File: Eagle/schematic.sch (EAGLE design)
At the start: 4 parts, among them IC1 ATMEGA328-20P

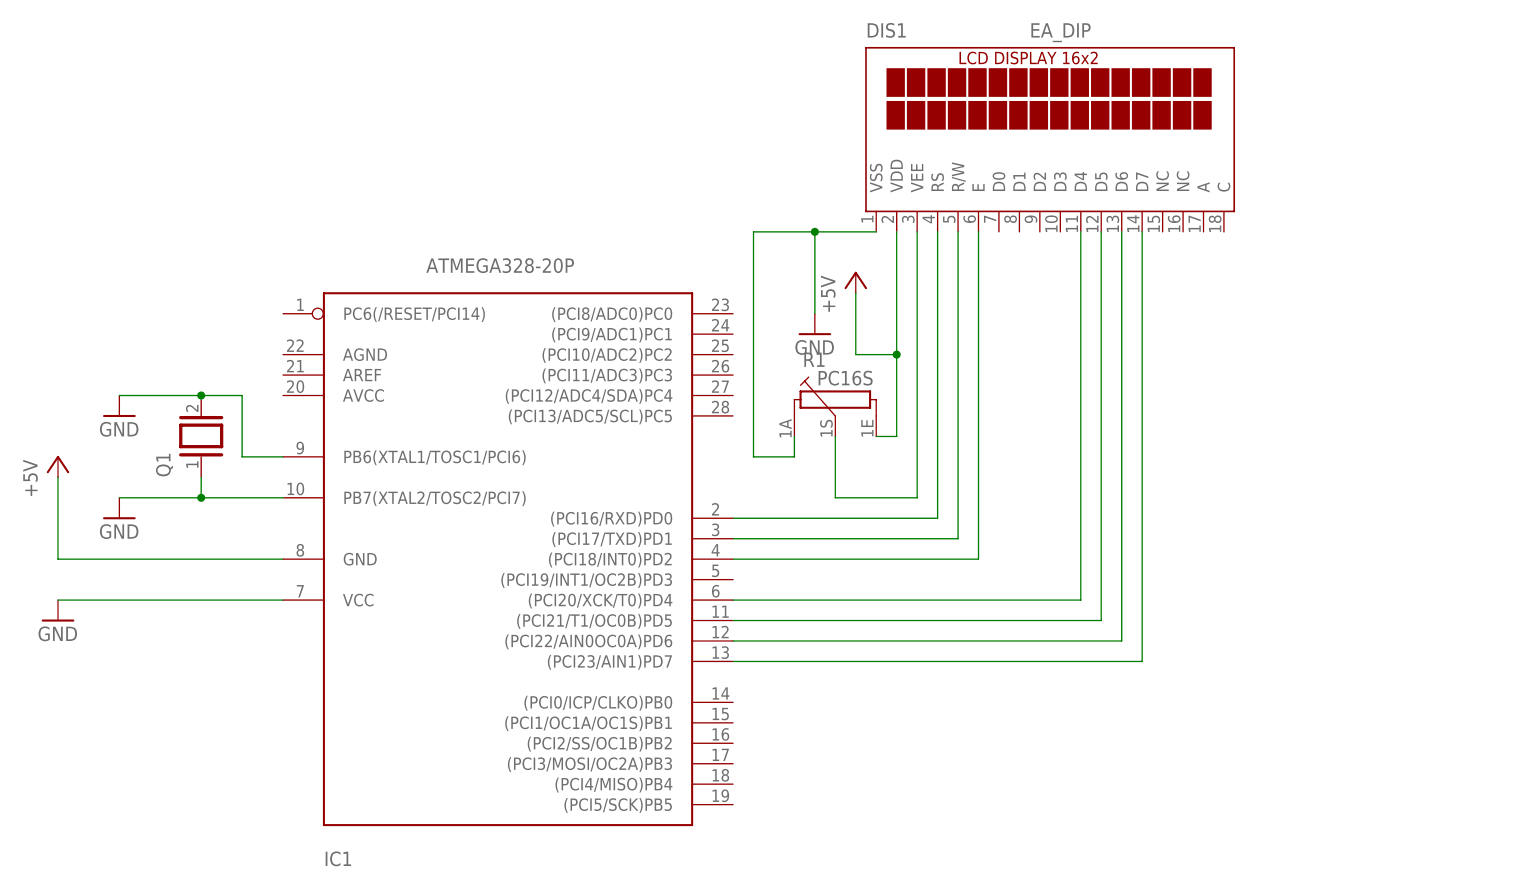
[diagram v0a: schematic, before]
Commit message: Add schematic file to the project
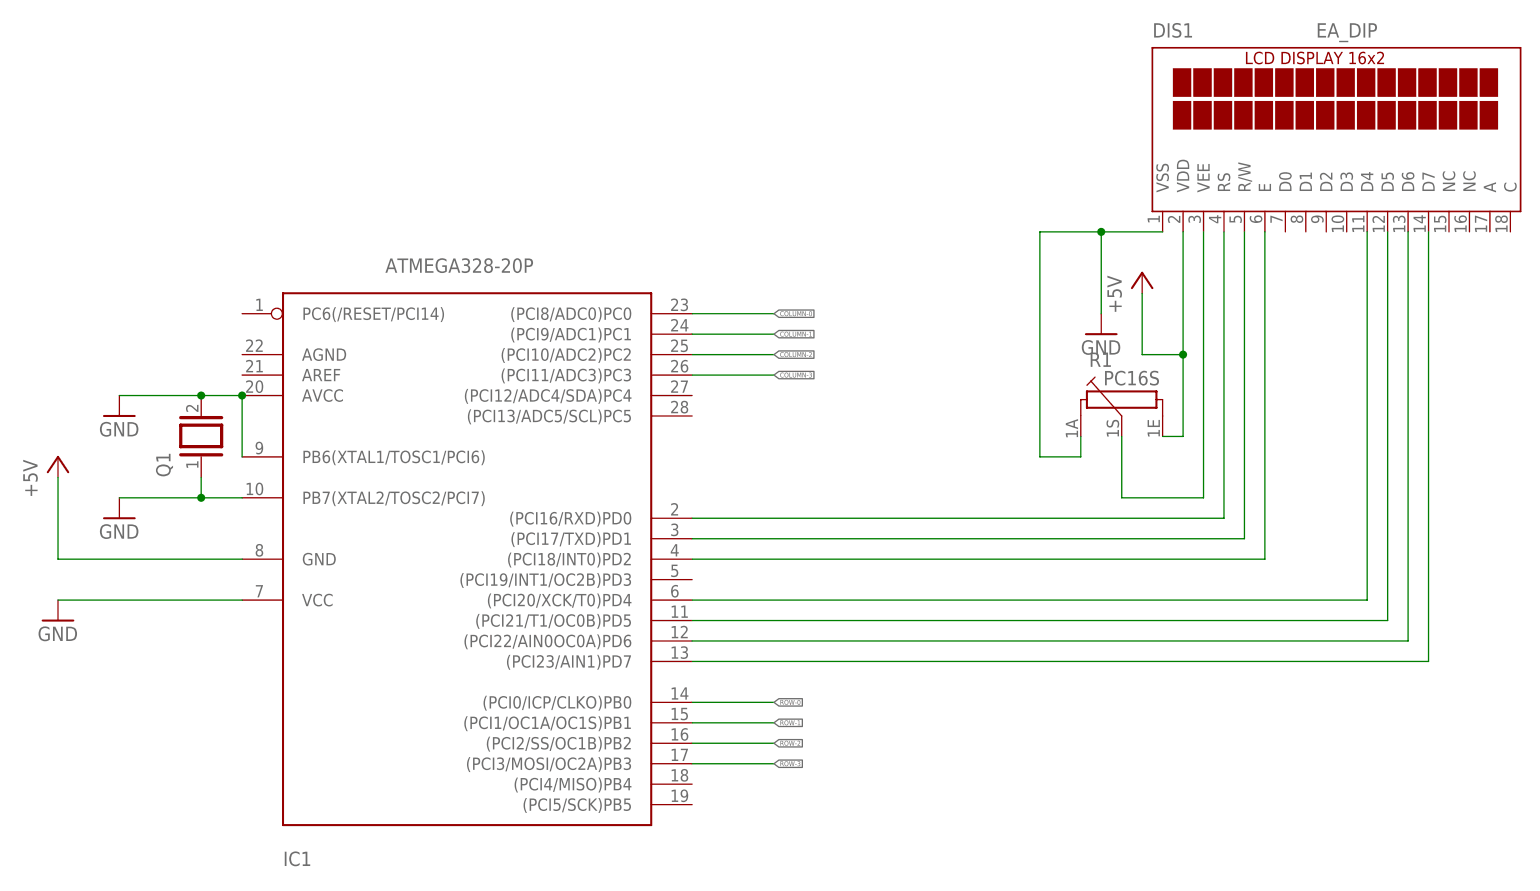
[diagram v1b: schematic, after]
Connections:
- net GND: now also IC1.AVCC
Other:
- moved on the sheet: DIS1, IC1, R1
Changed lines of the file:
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@@
 </plain>
 <instances>
-<instance part="IC1" gate="G$1" x="63.5" y="55.88"/>
-<instance part="DIS1" gate="G$1" x="134.62" y="104.14"/>
+<instance part="IC1" gate="G$1" x="58.42" y="55.88"/>
+<instance part="DIS1" gate="G$1" x="170.18" y="104.14"/>
 <instance part="GND1" gate="1" x="12.7" y="45.72"/>
 <instance part="P+1" gate="1" x="12.7" y="66.04"/>
-<instance part="P+2" gate="1" x="111.76" y="88.9"/>
-<instance part="GND2" gate="1" x="106.68" y="81.28"/>
-<instance part="R1" gate="G$1" x="109.22" y="73.66"/>
+<instance part="P+2" gate="1" x="147.32" y="88.9"/>
+<instance part="GND2" gate="1" x="142.24" y="81.28"/>
+<instance part="R1" gate="G$1" x="144.78" y="73.66"/>
 <instance part="Q1" gate="G$1" x="30.48" y="68.58" rot="R90"/>
 <instance part="GND3" gate="1" x="20.32" y="58.42"/>
@@
 <segment>
 <pinref part="IC1" gate="G$1" pin="VCC"/>
-<wire x1="40.64" y1="48.26" x2="12.7" y2="48.26" width="0.1524" layer="91"/>
+<wire x1="35.56" y1="48.26" x2="12.7" y2="48.26" width="0.1524" layer="91"/>
 <pinref part="GND1" gate="1" pin="GND"/>
 </segment>
@@
 <pinref part="DIS1" gate="G$1" pin="VSS"/>
 <pinref part="GND2" gate="1" pin="GND"/>
-<wire x1="114.3" y1="93.98" x2="106.68" y2="93.98" width="0.1524" layer="91"/>
-<wire x1="106.68" y1="93.98" x2="106.68" y2="83.82" width="0.1524" layer="91"/>
-<wire x1="106.68" y1="93.98" x2="99.06" y2="93.98" width="0.1524" layer="91"/>
-<junction x="106.68" y="93.98"/>
-<wire x1="99.06" y1="93.98" x2="99.06" y2="66.04" width="0.1524" layer="91"/>
-<wire x1="99.06" y1="66.04" x2="104.14" y2="66.04" width="0.1524" layer="91"/>
+<wire x1="149.86" y1="93.98" x2="142.24" y2="93.98" width="0.1524" layer="91"/>
+<wire x1="142.24" y1="93.98" x2="142.24" y2="83.82" width="0.1524" layer="91"/>
+<wire x1="142.24" y1="93.98" x2="134.62" y2="93.98" width="0.1524" layer="91"/>
+<junction x="142.24" y="93.98"/>
+<wire x1="134.62" y1="93.98" x2="134.62" y2="66.04" width="0.1524" layer="91"/>
+<wire x1="134.62" y1="66.04" x2="139.7" y2="66.04" width="0.1524" layer="91"/>
 <pinref part="R1" gate="G$1" pin="1A"/>
-<wire x1="104.14" y1="66.04" x2="104.14" y2="68.58" width="0.1524" layer="91"/>
+<wire x1="139.7" y1="66.04" x2="139.7" y2="68.58" width="0.1524" layer="91"/>
 </segment>
 <segment>
 <pinref part="IC1" gate="G$1" pin="PB6(XTAL1/TOSC1/PCI6)"/>
-<wire x1="40.64" y1="66.04" x2="35.56" y2="66.04" width="0.1524" layer="91"/>
 <wire x1="35.56" y1="66.04" x2="35.56" y2="73.66" width="0.1524" layer="91"/>
 <pinref part="Q1" gate="G$1" pin="2"/>
@@
 <pinref part="GND4" gate="1" pin="GND"/>
 <wire x1="30.48" y1="73.66" x2="20.32" y2="73.66" width="0.1524" layer="91"/>
+<pinref part="IC1" gate="G$1" pin="AVCC"/>
+<junction x="35.56" y="73.66"/>
 </segment>
 <segment>
 <pinref part="IC1" gate="G$1" pin="PB7(XTAL2/TOSC2/PCI7)"/>
 <pinref part="Q1" gate="G$1" pin="1"/>
-<wire x1="40.64" y1="60.96" x2="30.48" y2="60.96" width="0.1524" layer="91"/>
+<wire x1="35.56" y1="60.96" x2="30.48" y2="60.96" width="0.1524" layer="91"/>
 <wire x1="30.48" y1="60.96" x2="30.48" y2="63.5" width="0.1524" layer="91"/>
 <pinref part="GND3" gate="1" pin="GND"/>
@@
 <segment>
 <pinref part="IC1" gate="G$1" pin="GND"/>
-<wire x1="40.64" y1="53.34" x2="12.7" y2="53.34" width="0.1524" layer="91"/>
+<wire x1="35.56" y1="53.34" x2="12.7" y2="53.34" width="0.1524" layer="91"/>
 <wire x1="12.7" y1="53.34" x2="12.7" y2="63.5" width="0.1524" layer="91"/>
 <pinref part="P+1" gate="1" pin="+5V"/>
@@
 <segment>
 <pinref part="DIS1" gate="G$1" pin="VDD"/>
-<wire x1="116.84" y1="93.98" x2="116.84" y2="78.74" width="0.1524" layer="91"/>
-<wire x1="116.84" y1="78.74" x2="111.76" y2="78.74" width="0.1524" layer="91"/>
+<wire x1="152.4" y1="93.98" x2="152.4" y2="78.74" width="0.1524" layer="91"/>
+<wire x1="152.4" y1="78.74" x2="147.32" y2="78.74" width="0.1524" layer="91"/>
 <pinref part="P+2" gate="1" pin="+5V"/>
-<wire x1="111.76" y1="78.74" x2="111.76" y2="86.36" width="0.1524" layer="91"/>
+<wire x1="147.32" y1="78.74" x2="147.32" y2="86.36" width="0.1524" layer="91"/>
 <pinref part="R1" gate="G$1" pin="1E"/>
-<wire x1="114.3" y1="68.58" x2="116.84" y2="68.58" width="0.1524" layer="91"/>
-<wire x1="116.84" y1="68.58" x2="116.84" y2="78.74" width="0.1524" layer="91"/>
-<junction x="116.84" y="78.74"/>
+<wire x1="149.86" y1="68.58" x2="152.4" y2="68.58" width="0.1524" layer="91"/>
+<wire x1="152.4" y1="68.58" x2="152.4" y2="78.74" width="0.1524" layer="91"/>
+<junction x="152.4" y="78.74"/>
 </segment>
 </net>
@@
 <pinref part="IC1" gate="G$1" pin="(PCI16/RXD)PD0"/>
 <pinref part="DIS1" gate="G$1" pin="RS"/>
-<wire x1="96.52" y1="58.42" x2="121.92" y2="58.42" width="0.1524" layer="91"/>
-<wire x1="121.92" y1="58.42" x2="121.92" y2="93.98" width="0.1524" layer="91"/>
+<wire x1="91.44" y1="58.42" x2="157.48" y2="58.42" width="0.1524" layer="91"/>
+<wire x1="157.48" y1="58.42" x2="157.48" y2="93.98" width="0.1524" layer="91"/>
 </segment>
 </net>
@@
 <pinref part="IC1" gate="G$1" pin="(PCI17/TXD)PD1"/>
 <pinref part="DIS1" gate="G$1" pin="R/W"/>
-<wire x1="96.52" y1="55.88" x2="124.46" y2="55.88" width="0.1524" layer="91"/>
-<wire x1="124.46" y1="55.88" x2="124.46" y2="93.98" width="0.1524" layer="91"/>
+<wire x1="91.44" y1="55.88" x2="160.02" y2="55.88" width="0.1524" layer="91"/>
+<wire x1="160.02" y1="55.88" x2="160.02" y2="93.98" width="0.1524" layer="91"/>
 </segment>
 </net>
@@
 <pinref part="IC1" gate="G$1" pin="(PCI18/INT0)PD2"/>
 <pinref part="DIS1" gate="G$1" pin="E"/>
-<wire x1="96.52" y1="53.34" x2="127" y2="53.34" width="0.1524" layer="91"/>
-<wire x1="127" y1="53.34" x2="127" y2="93.98" width="0.1524" layer="91"/>
+<wire x1="91.44" y1="53.34" x2="162.56" y2="53.34" width="0.1524" layer="91"/>
+<wire x1="162.56" y1="53.34" x2="162.56" y2="93.98" width="0.1524" layer="91"/>
 </segment>
 </net>
@@
 <pinref part="IC1" gate="G$1" pin="(PCI23/AIN1)PD7"/>
 <pinref part="DIS1" gate="G$1" pin="D7"/>
-<wire x1="96.52" y1="40.64" x2="147.32" y2="40.64" width="0.1524" layer="91"/>
-<wire x1="147.32" y1="40.64" x2="147.32" y2="93.98" width="0.1524" layer="91"/>
+<wire x1="91.44" y1="40.64" x2="182.88" y2="40.64" width="0.1524" layer="91"/>
+<wire x1="182.88" y1="40.64" x2="182.88" y2="93.98" width="0.1524" layer="91"/>
 </segment>
 </net>
@@
 <pinref part="IC1" gate="G$1" pin="(PCI22/AIN0OC0A)PD6"/>
 <pinref part="DIS1" gate="G$1" pin="D6"/>
-<wire x1="96.52" y1="43.18" x2="144.78" y2="43.18" width="0.1524" layer="91"/>
-<wire x1="144.78" y1="43.18" x2="144.78" y2="93.98" width="0.1524" layer="91"/>
+<wire x1="91.44" y1="43.18" x2="180.34" y2="43.18" width="0.1524" layer="91"/>
+<wire x1="180.34" y1="43.18" x2="180.34" y2="93.98" width="0.1524" layer="91"/>
 </segment>
 </net>
@@
 <pinref part="IC1" gate="G$1" pin="(PCI21/T1/OC0B)PD5"/>
 <pinref part="DIS1" gate="G$1" pin="D5"/>
-<wire x1="96.52" y1="45.72" x2="142.24" y2="45.72" width="0.1524" layer="91"/>
-<wire x1="142.24" y1="45.72" x2="142.24" y2="93.98" width="0.1524" layer="91"/>
+<wire x1="91.44" y1="45.72" x2="177.8" y2="45.72" width="0.1524" layer="91"/>
+<wire x1="177.8" y1="45.72" x2="177.8" y2="93.98" width="0.1524" layer="91"/>
 </segment>
 </net>
@@
 <pinref part="IC1" gate="G$1" pin="(PCI20/XCK/T0)PD4"/>
 <pinref part="DIS1" gate="G$1" pin="D4"/>
-<wire x1="96.52" y1="48.26" x2="139.7" y2="48.26" width="0.1524" layer="91"/>
-<wire x1="139.7" y1="48.26" x2="139.7" y2="93.98" width="0.1524" layer="91"/>
+<wire x1="91.44" y1="48.26" x2="175.26" y2="48.26" width="0.1524" layer="91"/>
+<wire x1="175.26" y1="48.26" x2="175.26" y2="93.98" width="0.1524" layer="91"/>
 </segment>
 </net>
@@
 <segment>
 <pinref part="R1" gate="G$1" pin="1S"/>
-<wire x1="109.22" y1="68.58" x2="109.22" y2="60.96" width="0.1524" layer="91"/>
-<wire x1="109.22" y1="60.96" x2="119.38" y2="60.96" width="0.1524" layer="91"/>
+<wire x1="144.78" y1="68.58" x2="144.78" y2="60.96" width="0.1524" layer="91"/>
+<wire x1="144.78" y1="60.96" x2="154.94" y2="60.96" width="0.1524" layer="91"/>
 <pinref part="DIS1" gate="G$1" pin="VEE"/>
-<wire x1="119.38" y1="60.96" x2="119.38" y2="93.98" width="0.1524" layer="91"/>
+<wire x1="154.94" y1="60.96" x2="154.94" y2="93.98" width="0.1524" layer="91"/>
 </segment>
 </net>
+<net name="COLUMN-0" class="0">
+<segment>
+<wire x1="91.44" y1="83.82" x2="101.6" y2="83.82" width="0.1524" layer="91"/>
+<label x="101.6" y="83.82" size="0.6096" layer="95" xref="yes"/>
+</segment>
+</net>
+<net name="COLUMN-2" class="0">
+<segment>
+<wire x1="91.44" y1="78.74" x2="101.6" y2="78.74" width="0.1524" layer="91"/>
+<label x="101.6" y="78.74" size="0.6096" layer="95" xref="yes"/>
+</segment>
+</net>
+<net name="COLUMN-3" class="0">
+<segment>
+<wire x1="91.44" y1="76.2" x2="101.6" y2="76.2" width="0.1524" layer="91"/>
+<label x="101.6" y="76.2" size="0.6096" layer="95" xref="yes"/>
+</segment>
+</net>
+<net name="COLUMN-1" class="0">
+<segment>
+<wire x1="91.44" y1="81.28" x2="101.6" y2="81.28" width="0.1524" layer="91"/>
+<label x="101.6" y="81.28" size="0.6096" layer="95" xref="yes"/>
+</segment>
+</net>
+<net name="ROW-0" class="0">
+<segment>
+<wire x1="91.44" y1="35.56" x2="101.6" y2="35.56" width="0.1524" layer="91"/>
+<label x="101.6" y="35.56" size="0.6096" layer="95" xref="yes"/>
+</segment>
+</net>
+<net name="ROW-1" class="0">
+<segment>
+<wire x1="91.44" y1="33.02" x2="101.6" y2="33.02" width="0.1524" layer="91"/>
+<label x="101.6" y="33.02" size="0.6096" layer="95" xref="yes"/>
+</segment>
+</net>
+<net name="ROW-2" class="0">
+<segment>
+<wire x1="91.44" y1="30.48" x2="101.6" y2="30.48" width="0.1524" layer="91"/>
+<label x="101.6" y="30.48" size="0.6096" layer="95" xref="yes"/>
+</segment>
+</net>
+<net name="ROW-3" class="0">
+<segment>
+<wire x1="91.44" y1="27.94" x2="101.6" y2="27.94" width="0.1524" layer="91"/>
+<label x="101.6" y="27.94" size="0.6096" layer="95" xref="yes"/>
+</segment>
+</net>
